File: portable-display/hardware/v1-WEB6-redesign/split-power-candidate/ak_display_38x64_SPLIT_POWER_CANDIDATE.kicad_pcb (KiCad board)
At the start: 4 copper layers, 38 x 64 mm, 119 parts, among them J1 USB4105-GF-A-060, J2 1S LiPo + NTC, J3 DEBUG POGO, J4 KD024EGOIN152-01, J5 MicroSD, Q1 2N7002, Q2 2N7002, Q3 AO3401A, SW1 UP, SW2 DOWN, SW3 OK, SW4 BACK, SW5 POWER, SW6 FEL, U1 AXP2101, U10 TPS65631DPDR, U2 V851s, U4 LIS2DW12TR, U5 RV-3028-C7, U6 SN74LVC1G123DCTR, U8 TPS22918DBVR, U9 USBLC6-2SC6, Y1 24MHz 10ppm

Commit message: feat: update split-power PCB layout with refined footprints, routing verification data, and updated layout documentation.
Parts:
- U6: footprint Sameat:SSOP-8 -> Sameat:SN74LVC1G123_DCT8
- U8: footprint Sameat:SOT23-6 -> Sameat:TPS22918_DBV6
- U9: footprint Sameat:SOT23-6 -> Sameat:USBLC6-2SC6_SOT23-6
- moved C34 0.95 mm to (25.8, 29.8)
- moved C14 0.90 mm to (25.4, 31.3)
- moved C16 0.83 mm to (16.9, 34.8), turned to 0 degrees
- moved C26 0.52 mm to (29.3, 4.90)
- moved R1 0.46 mm to (14.3, 55.4)
- moved U8 0.34 mm to (5.80, 37.4)
- moved U9 0.23 mm to (16.8, 54.7)
- moved D10 0.20 mm to (24.3, 28.0)
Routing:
- net GND: track 182.6 -> 10.3 mm, vias 31 -> 44
- net 3V3: track 201.9 -> 131.2 mm, vias 16 -> 14
- net USB_CC2: track 88.9 -> 25.7 mm, vias 10 -> 3
- net SD_PWR_EN: track 2.40 -> 62.2 mm, vias 0 -> 8
- net DRAM_1V5: track 54.8 -> 104.1 mm, vias 3 -> 8
- net VSYS: track 97.0 -> 55.5 mm, vias 9 -> 11
- net LCD_EN: track 90.6 -> 51.0 mm, vias 6 -> 8
- net USB_DM: track 83.3 -> 47.5 mm
- net SD_D2: track 2.71 -> 26.8 mm, vias 0 -> 4
- net LCD_TE: track 0.00 -> 20.1 mm, vias 0 -> 2
- net 1V8: track 59.7 -> 41.7 mm, vias 9 -> 8
- net USB_DP: track 64.3 -> 48.9 mm
- net SD_DET: track 3.42 -> 18.2 mm, vias 0 -> 4
- net LCD_RST: track 0.00 -> 13.5 mm, vias 0 -> 2
- net SD_D0: track 0.00 -> 13.0 mm, vias 0 -> 3
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
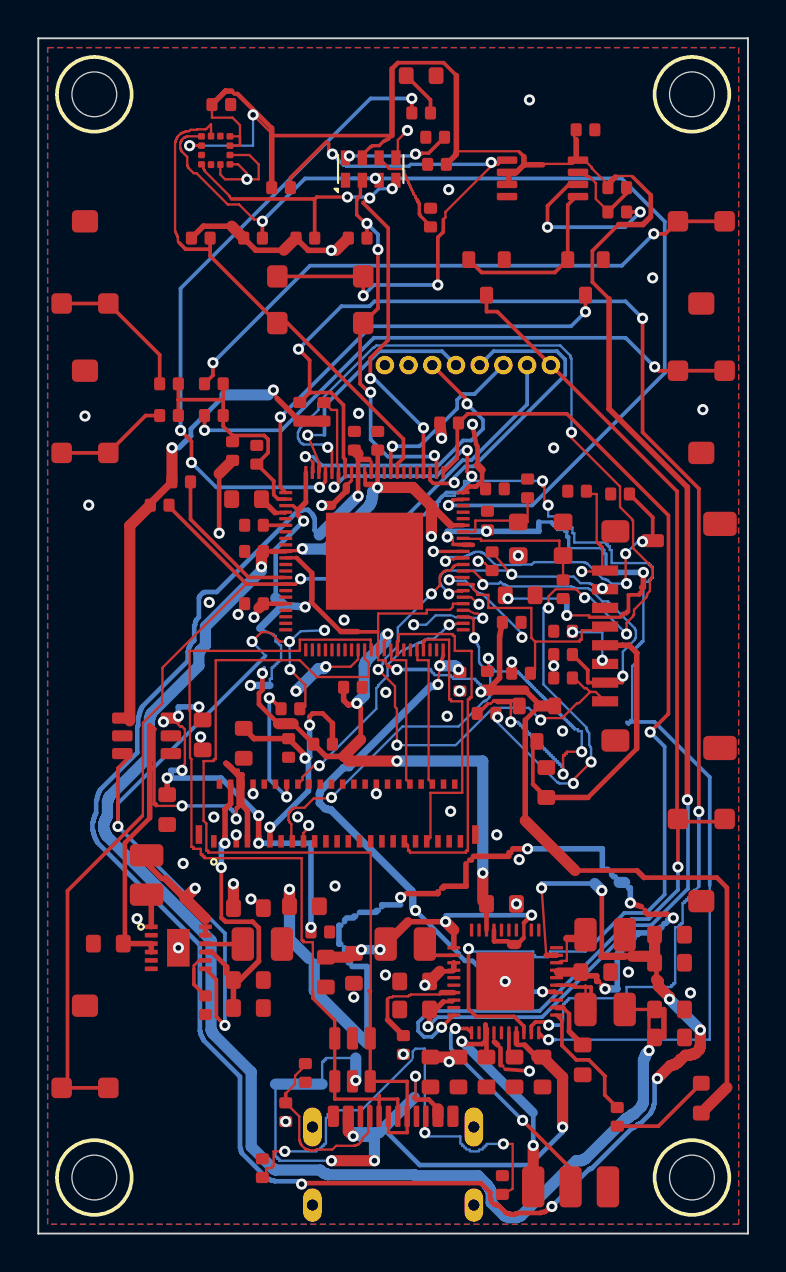
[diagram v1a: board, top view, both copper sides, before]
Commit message: fix(pcb): repair U1/U2 land patterns and re-route escapes for split-power layout
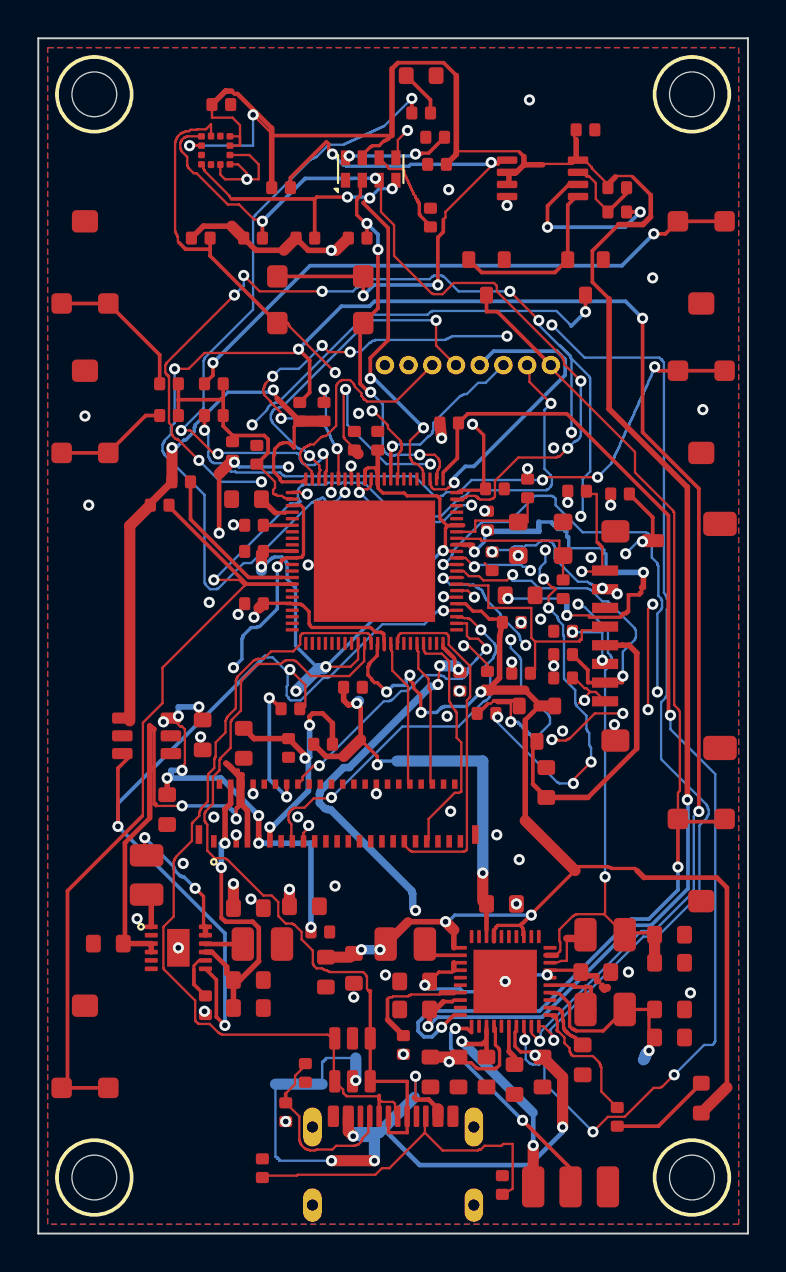
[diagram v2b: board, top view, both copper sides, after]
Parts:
- moved C38 0.40 mm to (25.5, 55.8)
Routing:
- net CORE_0V93: track 125.9 -> 67.4 mm, vias 13 -> 9
- net DRAM_1V5: track 104.1 -> 54.1 mm, vias 8 -> 7
- net VSYS: track 55.5 -> 29.1 mm, vias 11 -> 7
- net PMIC_SDA: track 77.3 -> 98.6 mm, vias 4 -> 6
- net SD_D0: track 13.0 -> 34.3 mm, vias 3 -> 8
- net SD_PWR_EN: track 62.2 -> 79.2 mm, vias 8 -> 16
- net BOOT0: track 60.5 -> 73.8 mm, vias 1 -> 2
- net I2C0_SCL: track 57.5 -> 46.2 mm, vias 3 -> 4
- net USB_CC2: track 25.7 -> 18.7 mm, vias 3 -> 0
- net PMIC_IRQ_N: track 57.1 -> 63.3 mm, vias 2 -> 4
- net WAKE_PULSE_N: track 23.7 -> 29.3 mm, vias 2 -> 3
- net USB_DP: track 48.9 -> 43.5 mm
- net SD_PWR_GATE: track 23.2 -> 18.3 mm, vias 4 -> 3
- net UART0_RX: track 13.6 -> 18.5 mm, vias 1 -> 2
- net SD_D2: track 26.8 -> 31.5 mm, vias 4 -> 3
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
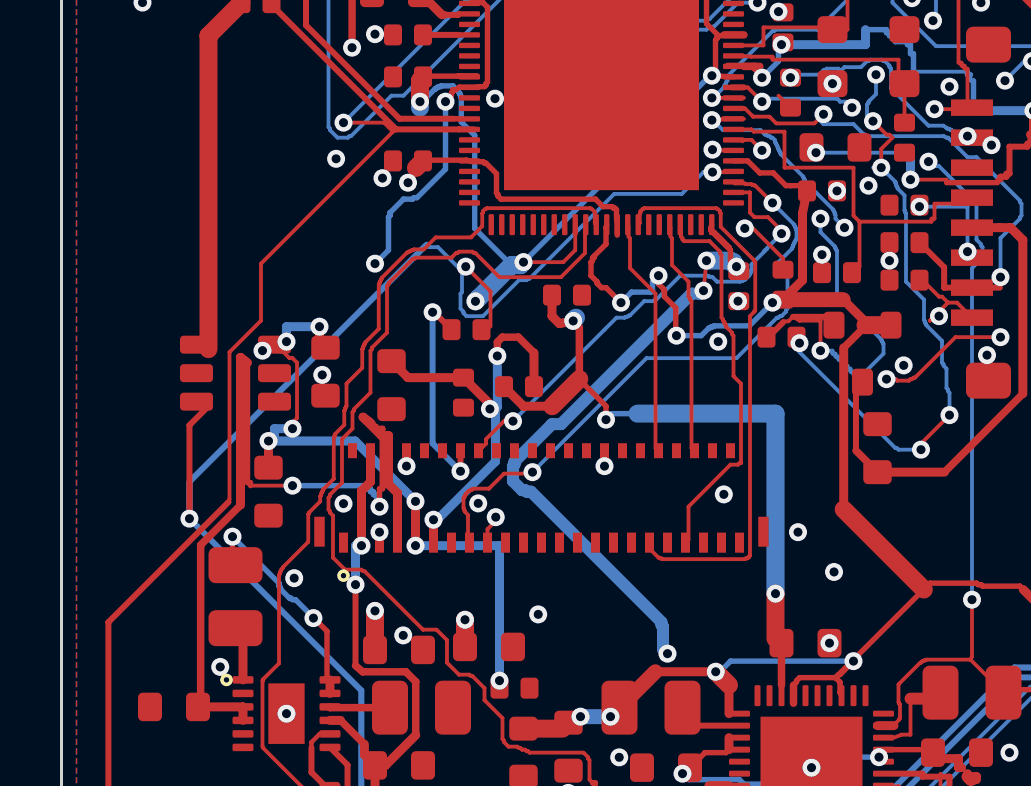
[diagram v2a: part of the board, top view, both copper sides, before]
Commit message: fix: resolve screen RESET/TE level matching
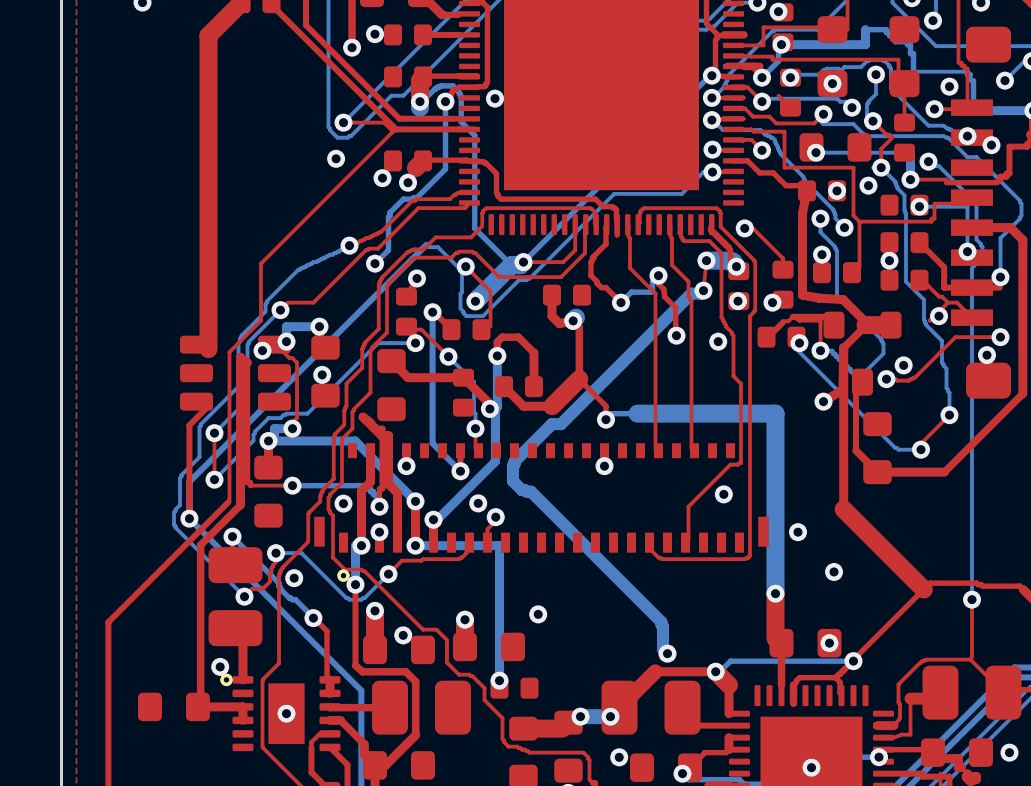
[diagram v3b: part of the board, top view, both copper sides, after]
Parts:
- added R32: 10k, Sameat:0402, F.Cu at (11.5, 35.3)
- R20: value 100k -> 10k
- R21: value 10k -> 100
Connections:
- R20 pad 1: 3V3 -> GND
- U2 pad 2: LCD_RST -> unconnected-(U2-PD19-Pad2)
- U2 pad 3: LCD_TE -> unconnected-(U2-PD20-Pad3)
- U2 pad 65: unconnected-(U2-PA9-Pad65) -> LCD_TE
- U2 pad 66: unconnected-(U2-PA8-Pad66) -> LCD_RST
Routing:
- net LCD_RST: track 16.2 -> 29.1 mm, vias 2 -> 6
- net LCD_TE: track 20.9 -> 30.5 mm, vias 2 -> 4
- net 3V3: track 134.5 -> 137.8 mm
- net GND: track 9.92 -> 10.6 mm, vias 52 -> 54

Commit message: fix(hardware): extend automatic wake pulse to nominal 3 seconds
Use a 910k resistor and 3.3uF 0805 timing capacitor, bind JLCPCB parts, and reroute the timing nets. Synchronize schematics, local footprint and independent component requirements. Physical timing and retrigger behavior remain subject to validation.
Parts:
- C23: value 100n -> 3.3u; footprint Sameat:0402 -> Sameat:C_0805_2012Metric
- R12: value 820k -> 910k
- moved C23 3.11 mm to (32.0, 6.35)
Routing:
- net WAKE_CEXT: track 9.18 -> 6.27 mm
- net WAKE_REXT: track 4.82 -> 6.83 mm, vias 0 -> 2

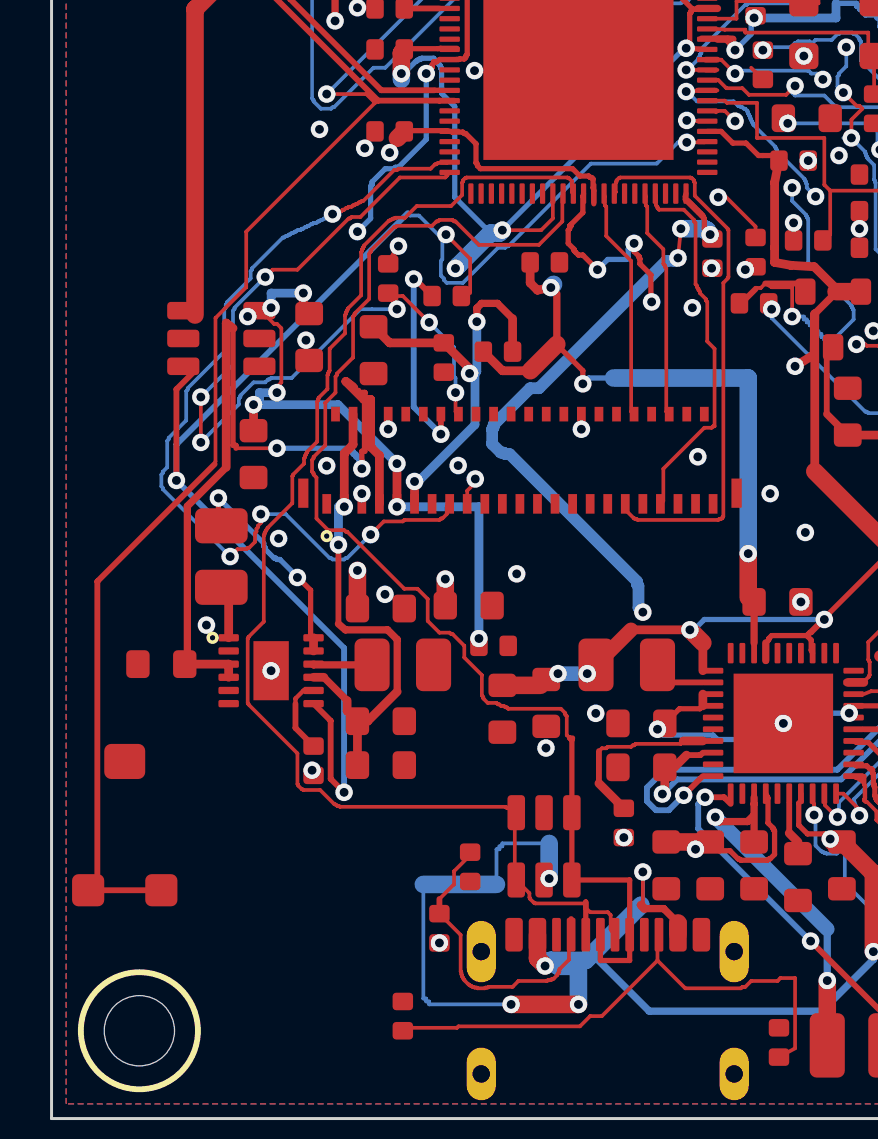
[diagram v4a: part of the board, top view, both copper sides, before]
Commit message: fix: repair USB routing by swapping DP/DM pins on U9 and updating layout files
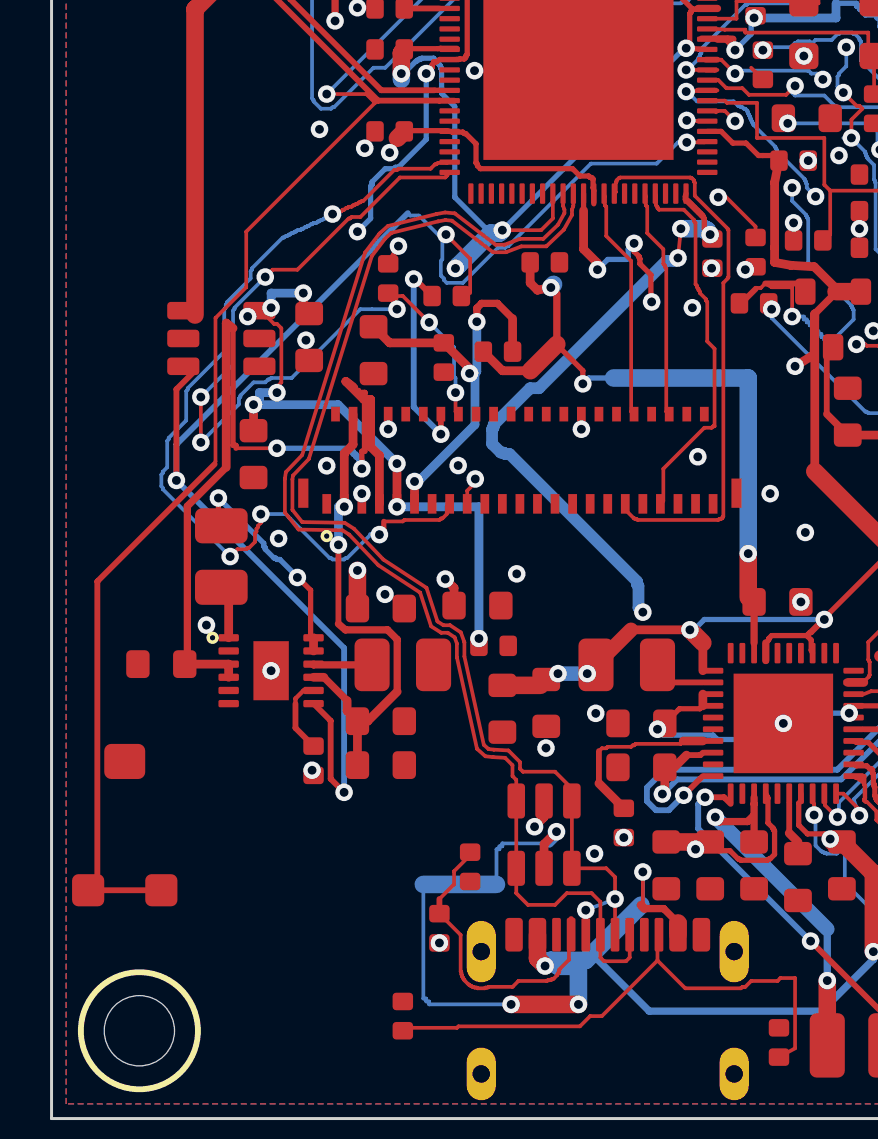
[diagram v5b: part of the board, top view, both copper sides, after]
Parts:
- moved U9 0.40 mm to (16.8, 54.3)
- moved C47 0.30 mm to (14.6, 46.5)
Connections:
- U9 pad 1: USB_DP -> USB_DM
- U9 pad 3: USB_DM -> USB_DP
- U9 pad 4: USB_DM -> USB_DP
- U9 pad 6: USB_DP -> USB_DM
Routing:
- net USB_DM: track 45.7 -> 41.7 mm, vias 0 -> 2
- net GND: track 10.6 -> 11.6 mm, vias 54 -> 56
- net VBUS: track 46.7 -> 47.4 mm
- net USB_DP: track 43.5 -> 42.9 mm
- net 3V3: track 137.8 -> 137.2 mm
